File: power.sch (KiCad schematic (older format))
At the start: 6 parts, among them J7 USB_B_Mini, J8 Screw_Terminal_01x02, U1 L78L05_TO92

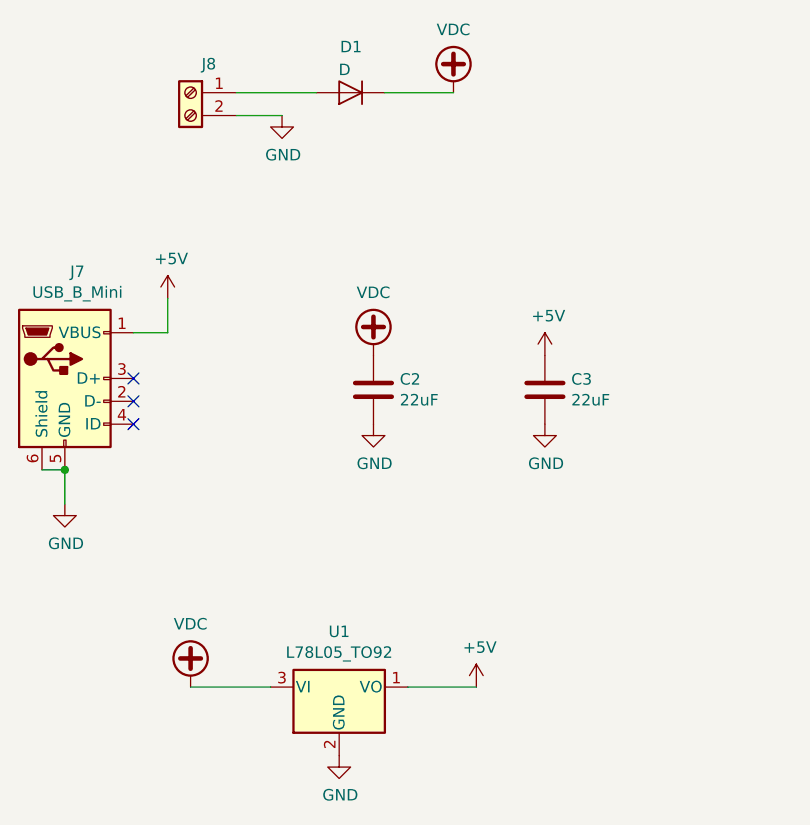
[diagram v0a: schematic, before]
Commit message: Added capacitor to stabilize the LEDs' 5V supply
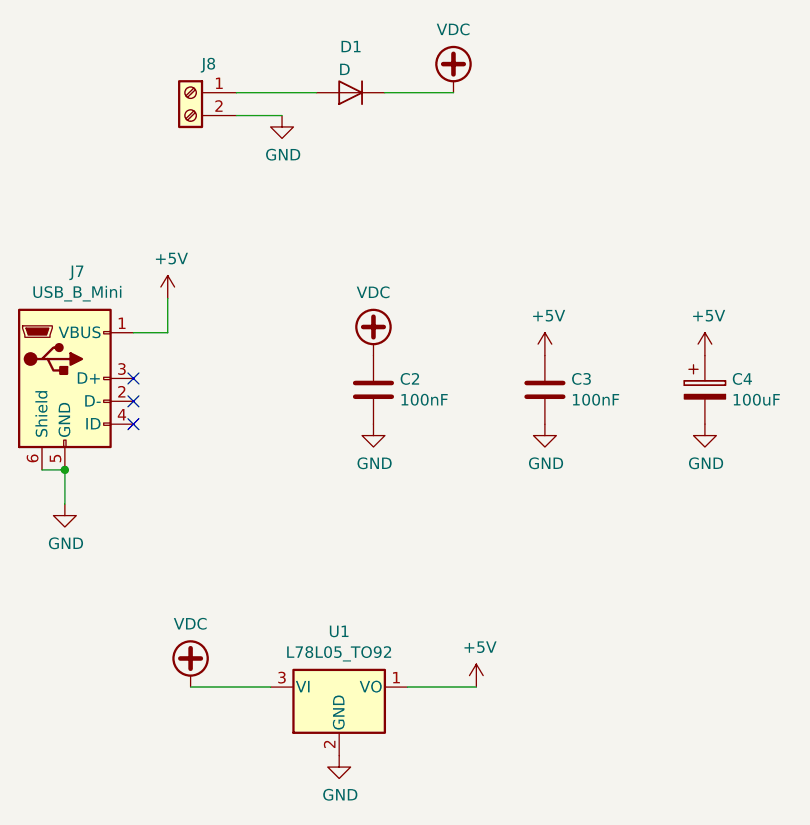
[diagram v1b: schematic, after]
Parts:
- added C4: 100uF, Capacitor_THT:CP_Radial_D8.0mm_P3.80mm, symbol Device:CP
- C2, C3: value 22uF -> 100nF
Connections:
- net +5V: now also C4.1
- net GND: now also C4.2
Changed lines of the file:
@@
 AR Path="/5C023B47/5C0259E0" Ref="C3"  Part="1"
 F 0 "C3" H 7315 3296 50  0000 L CNN
-F 1 "22uF" H 7315 3205 50  0000 L CNN
+F 1 "100nF" H 7315 3205 50  0000 L CNN
 F 2 "Capacitor_SMD:C_0805_2012Metric_Pad1.15x1.40mm_HandSolder" H 7238 3100 50  0001 C CNN
 F 3 "~" H 7200 3250 50  0001 C CNN
@@
 AR Path="/5C023B47/5C0259E8" Ref="C2"  Part="1"
 F 0 "C2" H 6565 3296 50  0000 L CNN
-F 1 "22uF" H 6565 3205 50  0000 L CNN
+F 1 "100nF" H 6565 3205 50  0000 L CNN
 F 2 "Capacitor_SMD:C_0805_2012Metric_Pad1.15x1.40mm_HandSolder" H 6488 3100 50  0001 C CNN
 F 3 "~" H 6450 3250 50  0001 C CNN
@@
 	1    0    0    -1
 $EndComp
+$Comp
+L power:+5V #PWR016
+U 1 1 5C04436D
+P 7900 3100
+F 0 "#PWR016" H 7900 2950 50  0001 C CNN
+F 1 "+5V" H 7915 3273 50  0000 C CNN
+F 2 "" H 7900 3100 50  0001 C CNN
+F 3 "" H 7900 3100 50  0001 C CNN
+	1    7900 3100
+	1    0    0    -1
+$EndComp
+$Comp
+L power:GND #PWR?
+U 1 1 5C044373
+P 7900 3400
+AR Path="/5C044373" Ref="#PWR?"  Part="1"
+AR Path="/5C023B47/5C044373" Ref="#PWR018"  Part="1"
+F 0 "#PWR018" H 7900 3150 50  0001 C CNN
+F 1 "GND" H 7905 3227 50  0000 C CNN
+F 2 "" H 7900 3400 50  0001 C CNN
+F 3 "" H 7900 3400 50  0001 C CNN
+	1    7900 3400
+	1    0    0    -1
+$EndComp
+$Comp
+L Device:CP C4
+U 1 1 5C0446DB
+P 7900 3250
+F 0 "C4" H 8018 3296 50  0000 L CNN
+F 1 "100uF" H 8018 3205 50  0000 L CNN
+F 2 "Capacitor_THT:CP_Radial_D8.0mm_P3.80mm" H 7938 3100 50  0001 C CNN
+F 3 "~" H 7900 3250 50  0001 C CNN
+	1    7900 3250
+	1    0    0    -1
+$EndComp
